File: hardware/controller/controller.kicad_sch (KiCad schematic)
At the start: 14 parts, among them J1 Conn_01x02_Pin, J2 Conn_01x02_Pin, J3 Conn_01x02_Pin, J4 Conn_01x02_Pin

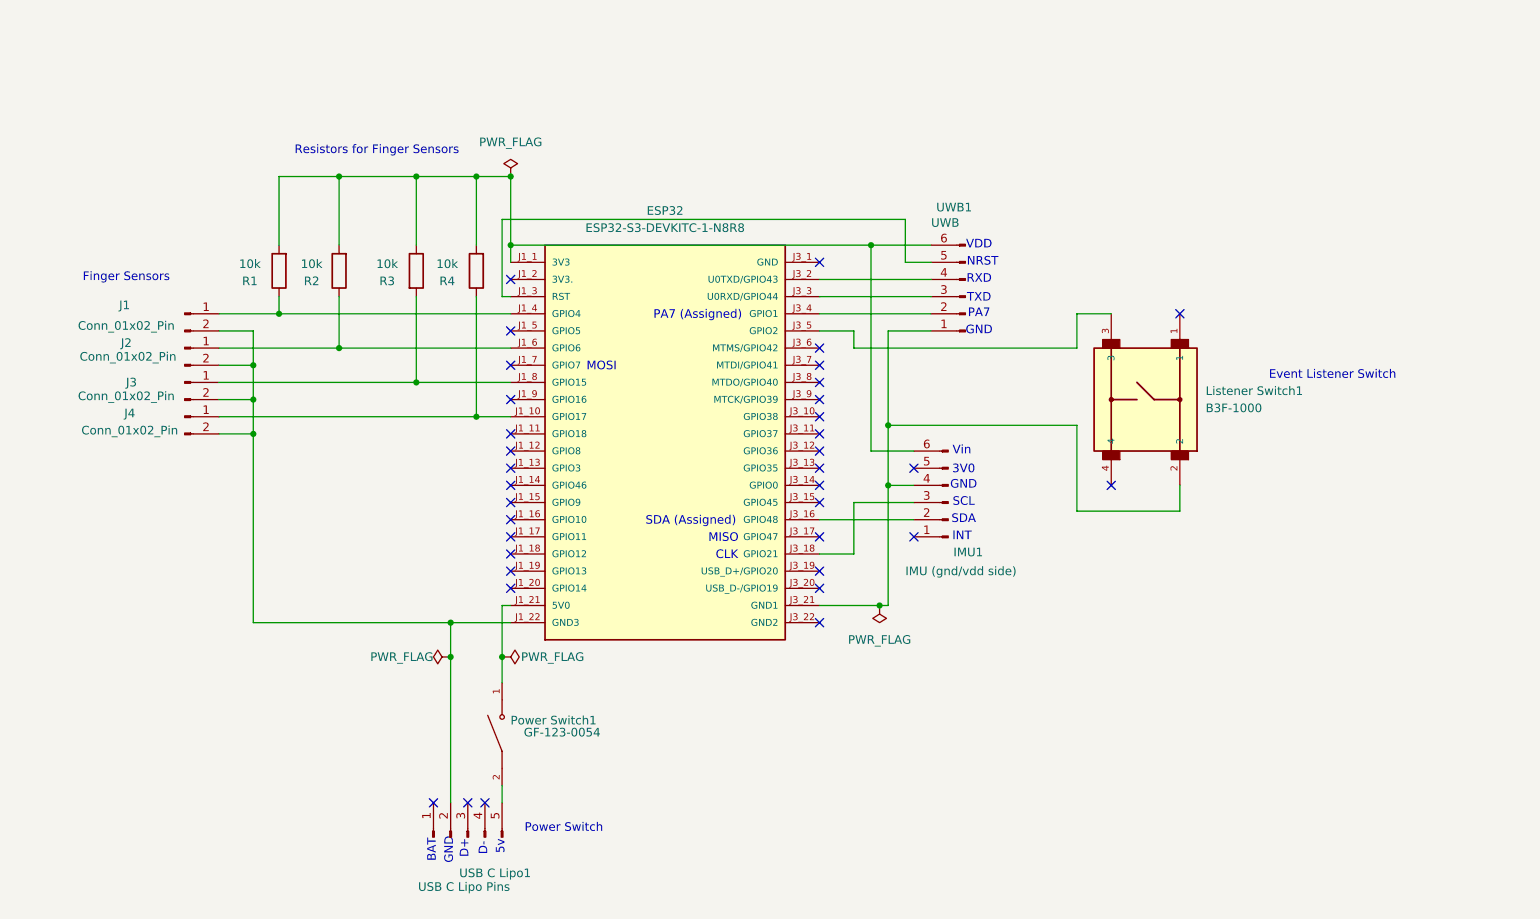
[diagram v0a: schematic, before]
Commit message: routing and screw hole placement done
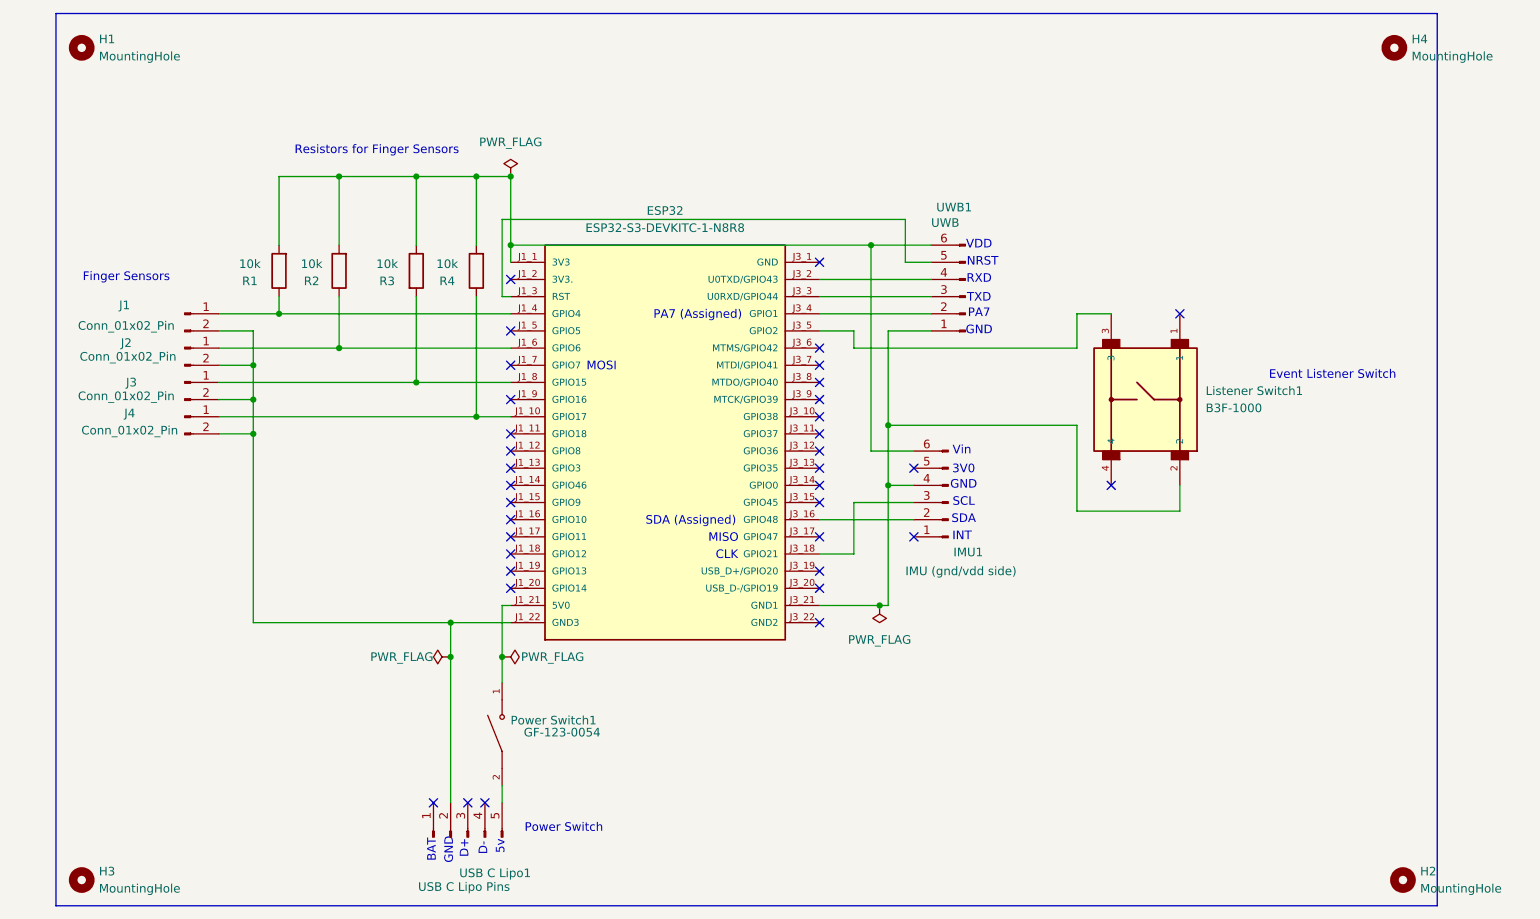
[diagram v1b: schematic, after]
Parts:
- added H1, H2, H3, H4: MountingHole, MountingHole:MountingHole_3.2mm_M3, symbol Mechanical:MountingHole

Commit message: edits made, PCB ready for 1st run
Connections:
- net at ESP32.J1_3 (RST): no longer UWB1.5 (Pin_5)
- net at ESP32.J3_2 (U0TXD/GPIO43): now also UWB1.5 (Pin_5); no longer UWB1.4 (Pin_4)
- net at ESP32.J3_3 (U0RXD/GPIO44): now also UWB1.4 (Pin_4); no longer UWB1.3 (Pin_3)
- net at ESP32.J3_4 (GPIO1): now also UWB1.3 (Pin_3); no longer UWB1.2 (Pin_2)
- net at ESP32.J3_5 (GPIO2): now also UWB1.2 (Pin_2); no longer Listener Switch1.3
- net at ESP32.J3_6 (MTMS/GPIO42): now also Listener Switch1.3
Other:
- moved on the sheet: Listener Switch1, UWB1

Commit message: added fab files
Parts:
- removed Listener Switch1: B3F-1000, B3F_1000:SW_B3F-1000, symbol B3F-1000:B3F-1000
- removed Power Switch1: GF-123-0054, GF_123_0054:SW_GF-123-0054, symbol GF-123-0054:GF-123-0054
- added Listener Switch: B3F-1000, Omron Tactile Button Small B3f-1000:SW_B3F-1000, symbol Omron Tactile Button Small:B3F-1000
- added Power Switch: GF-123-0054, On/Off Switch:SW_GF-123-0054, symbol On/Off Switch GF-123-0054:GF-123-0054
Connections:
- net at ESP32.J1_21 (5V0): now also Power Switch.1
- net at ESP32.J3_21 (GND1), IMU1.4 (Pin_4), UWB1.1 (Pin_1): now also Listener Switch.2
- net at ESP32.J3_6 (MTMS/GPIO42): now also Listener Switch.3
- net at USB C Lipo1.5 (Pin_5): now also Power Switch.2
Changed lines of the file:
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@@
+	)
+	(symbol
+		(lib_id "Omron Tactile Button Small:B3F-1000")
+		(at 364.49 195.58 90)
+		(unit 1)
+		(exclude_from_sim no)
+		(in_bom yes)
+		(on_board yes)
+		(dnp no)
+		(fields_autoplaced yes)
+		(property "Reference" "Listener Switch"
+			(at 373.38 194.3114 90)
+			(effects
+				(font
+					(size 1.27 1.27)
+				)
+				(justify right)
+			)
+		)
+		(property "Value" "B3F-1000"
+			(at 373.38 196.8514 90)
+			(effects
+				(font
+					(size 1.27 1.27)
+				)
+				(justify right)
+			)
+		)
+		(property "Footprint" "Omron Tactile Button Small B3f-1000:SW_B3F-1000"
+			(at 364.49 195.58 0)
+			(effects
+				(font
+					(size 1.27 1.27)
+				)
+				(justify bottom)
+				(hide yes)
+			)
+		)
+		(property "Datasheet" ""
+			(at 364.49 195.58 0)
+			(effects
+				(font
+					(size 1.27 1.27)
+				)
+				(hide yes)
+			)
+		)
+		(property "Description" ""
+			(at 364.49 195.58 0)
+			(effects
+				(font
+					(size 1.27 1.27)
+				)
+				(hide yes)
+			)
+		)
+		(property "MANUFACTURER" "Omron"
+			(at 364.49 195.58 0)
+			(effects
+				(font
+					(size 1.27 1.27)
+				)
+				(justify bottom)
+				(hide yes)
+			)
+		)
+		(pin "2"
+		)
+		(pin "1"
+		)
+		(pin "3"
+		)
+		(pin "4"
+		)
+		(instances
+			(project ""
+				(path "/50de191a-06b5-4968-8f0c-17f7744c4812"
+					(reference "Listener Switch")
+					(unit 1)
+				)
+			)
+		)
 	)
 	(symbol
@@
 	)
 	(symbol
+		(lib_id "On/Off Switch GF-123-0054:GF-123-0054")
+		(at 269.24 242.57 90)
+		(unit 1)
+		(exclude_from_sim no)
+		(in_bom yes)
+		(on_board yes)
+		(dnp no)
+		(fields_autoplaced yes)
+		(property "Reference" "Power Switch"
+			(at 270.51 241.2999 90)
+			(effects
+				(font
+					(size 1.27 1.27)
+				)
+				(justify right)
+			)
+		)
+		(property "Value" "GF-123-0054"
+			(at 270.51 243.8399 90)
+			(effects
+				(font
+					(size 1.27 1.27)
+				)
+				(justify right)
+			)
+		)
+		(property "Footprint" "On/Off Switch:SW_GF-123-0054"
+			(at 269.24 242.57 0)
+			(effects
+				(font
+					(size 1.27 1.27)
+				)
+				(justify bottom)
+				(hide yes)
+			)
+		)
+		(property "Datasheet" ""
+			(at 269.24 242.57 0)
+			(effects
+				(font
+					(size 1.27 1.27)
+				)
+				(hide yes)
+			)
+		)
+		(property "Description" ""
+			(at 269.24 242.57 0)
+			(effects
+				(font
+					(size 1.27 1.27)
+				)
+				(hide yes)
+			)
+		)
+		(property "PARTREV" "May 20, 2003"
+			(at 269.24 242.57 0)
+			(effects
+				(font
+					(size 1.27 1.27)
+				)
+				(justify bottom)
+				(hide yes)
+			)
+		)
+		(property "MANUFACTURER" "CW Industries"
+			(at 269.24 242.57 0)
+			(effects
+				(font
+					(size 1.27 1.27)
+				)
+				(justify bottom)
+				(hide yes)
+			)
+		)
+		(property "MAXIMUM_PACKAGE_HIEGHT" "14.96 mm"
+			(at 269.24 242.57 0)
+			(effects
+				(font
+					(size 1.27 1.27)
+				)
+				(justify bottom)
+				(hide yes)
+			)
+		)
+		(property "STANDARD" "Manufacturer Recommendations"
+			(at 269.24 242.57 0)
+			(effects
+				(font
+					(size 1.27 1.27)
+				)
+				(justify bottom)
+				(hide yes)
+			)
+		)
+		(pin "2"
+		)
+		(pin "1"
+		)
+		(instances
+			(project ""
+				(path "/50de191a-06b5-4968-8f0c-17f7744c4812"
+					(reference "Power Switch")
+					(unit 1)
+				)
+			)
+		)
+	)
+	(symbol
 		(lib_id "Connector:Conn_01x06_Pin")
 		(at 335.28 208.28 180)
@@
 	)
 	(symbol
-		(lib_id "GF-123-0054:GF-123-0054")
-		(at 269.24 242.57 90)
-		(unit 1)
-		(exclude_from_sim no)
-		(in_bom yes)
-		(on_board yes)
-		(dnp no)
-		(property "Reference" "Power Switch1"
-			(at 276.86 240.538 90)
-			(effects
-				(font
-					(size 1.27 1.27)
-				)
-			)
-		)
-		(property "Value" "GF-123-0054"
-			(at 278.13 242.316 90)
-			(effects
-				(font
-					(size 1.27 1.27)
-				)
-			)
-		)
-		(property "Footprint" "GF_123_0054:SW_GF-123-0054"
-			(at 269.24 242.57 0)
-			(effects
-				(font
-					(size 1.27 1.27)
-				)
-				(justify bottom)
-				(hide yes)
-			)
-		)
-		(property "Datasheet" ""
-			(at 269.24 242.57 0)
-			(effects
-				(font
-					(size 1.27 1.27)
-				)
-				(hide yes)
-			)
-		)
-		(property "Description" ""
-			(at 269.24 242.57 0)
-			(effects
-				(font
-					(size 1.27 1.27)
-				)
-				(hide yes)
-			)
-		)
-		(property "PARTREV" "May 20, 2003"
-			(at 269.24 242.57 0)
-			(effects
-				(font
-					(size 1.27 1.27)
-				)
-				(justify bottom)
-				(hide yes)
-			)
-		)
-		(property "MANUFACTURER" "CW Industries"
-			(at 269.24 242.57 0)
-			(effects
-				(font
-					(size 1.27 1.27)
-				)
-				(justify bottom)
-				(hide yes)
-			)
-		)
-		(property "MAXIMUM_PACKAGE_HIEGHT" "14.96 mm"
-			(at 269.24 242.57 0)
-			(effects
-				(font
-					(size 1.27 1.27)
-				)
-				(justify bottom)
-				(hide yes)
-			)
-		)
-		(property "STANDARD" "Manufacturer Recommendations"
-			(at 269.24 242.57 0)
-			(effects
-				(font
-					(size 1.27 1.27)
-				)
-				(justify bottom)
-				(hide yes)
-			)
-		)
-		(pin "1"
-		)
-		(pin "2"
-		)
-		(instances
-			(project ""
-				(path "/50de191a-06b5-4968-8f0c-17f7744c4812"
-					(reference "Power Switch1")
-					(unit 1)
-				)
-			)
-		)
-	)
-	(symbol
 		(lib_id "Mechanical:MountingHole")
 		(at 402.59 264.16 0)
@@
 					(unit 1)
 				)
-			)
-		)
-	)
-	(symbol
-		(lib_id "B3F-1000:B3F-1000")
-		(at 364.49 195.58 90)
-		(unit 1)
-		(exclude_from_sim no)
-		(in_bom yes)
-		(on_board yes)
-		(dnp no)
-		(fields_autoplaced yes)
-		(property "Reference" "Listener Switch1"
-			(at 373.38 194.3114 90)
-			(effects
-				(font
-					(size 1.27 1.27)
-				)
-				(justify right)
-			)
-		)
-		(property "Value" "B3F-1000"
-			(at 373.38 196.8514 90)
-			(effects
-				(font
-					(size 1.27 1.27)
-				)
-				(justify right)
-			)
-		)
-		(property "Footprint" "B3F_1000:SW_B3F-1000"
-			(at 364.49 195.58 0)
-			(effects
-				(font
-					(size 1.27 1.27)
-				)
-				(justify bottom)
-				(hide yes)
-			)
-		)
-		(property "Datasheet" ""
-			(at 364.49 195.58 0)
-			(effects
-				(font
-					(size 1.27 1.27)
-				)
-				(hide yes)
-			)
-		)
-		(property "Description" ""
-			(at 364.49 195.58 0)
-			(effects
-				(font
-					(size 1.27 1.27)
-				)
-				(hide yes)
-			)
-		)
-		(property "MANUFACTURER" "Omron"
-			(at 364.49 195.58 0)
-			(effects
-				(font
-					(size 1.27 1.27)
-				)
-				(justify bottom)
-				(hide yes)
-			)
-		)
-		(pin "2"
-		)
-		(pin "3"
-		)
-		(pin "1"
-		)
-		(pin "4"
-		)
-		(instances
-			(project ""
-				(path "/50de191a-06b5-4968-8f0c-17f7744c4812"
-					(reference "Listener Switch1")
-					(unit 1)
-				)

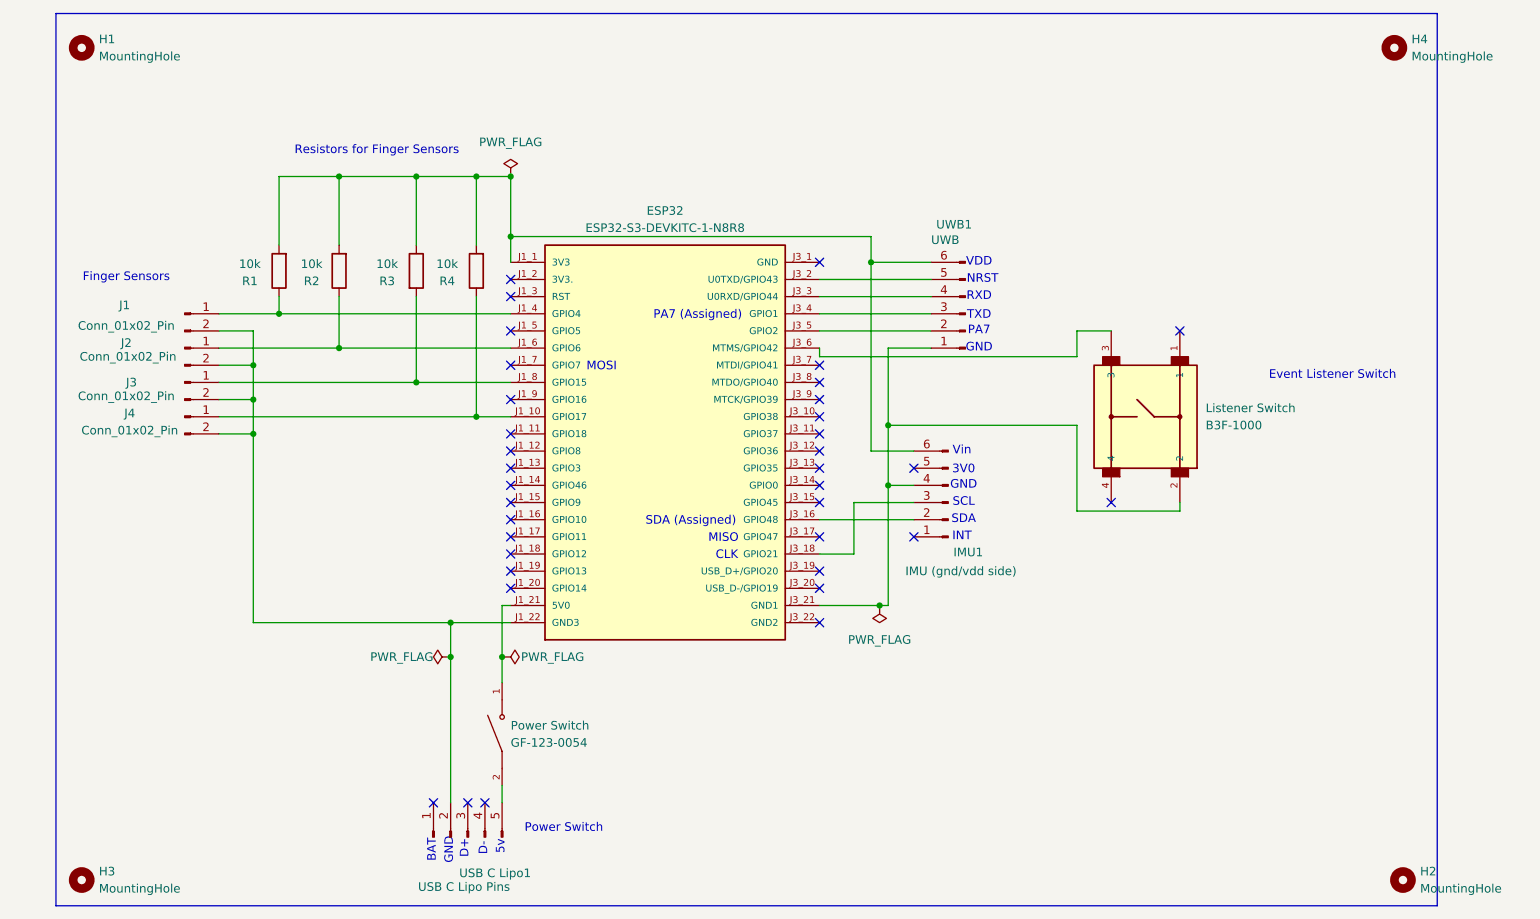
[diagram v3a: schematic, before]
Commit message: schem fixed, ready to route
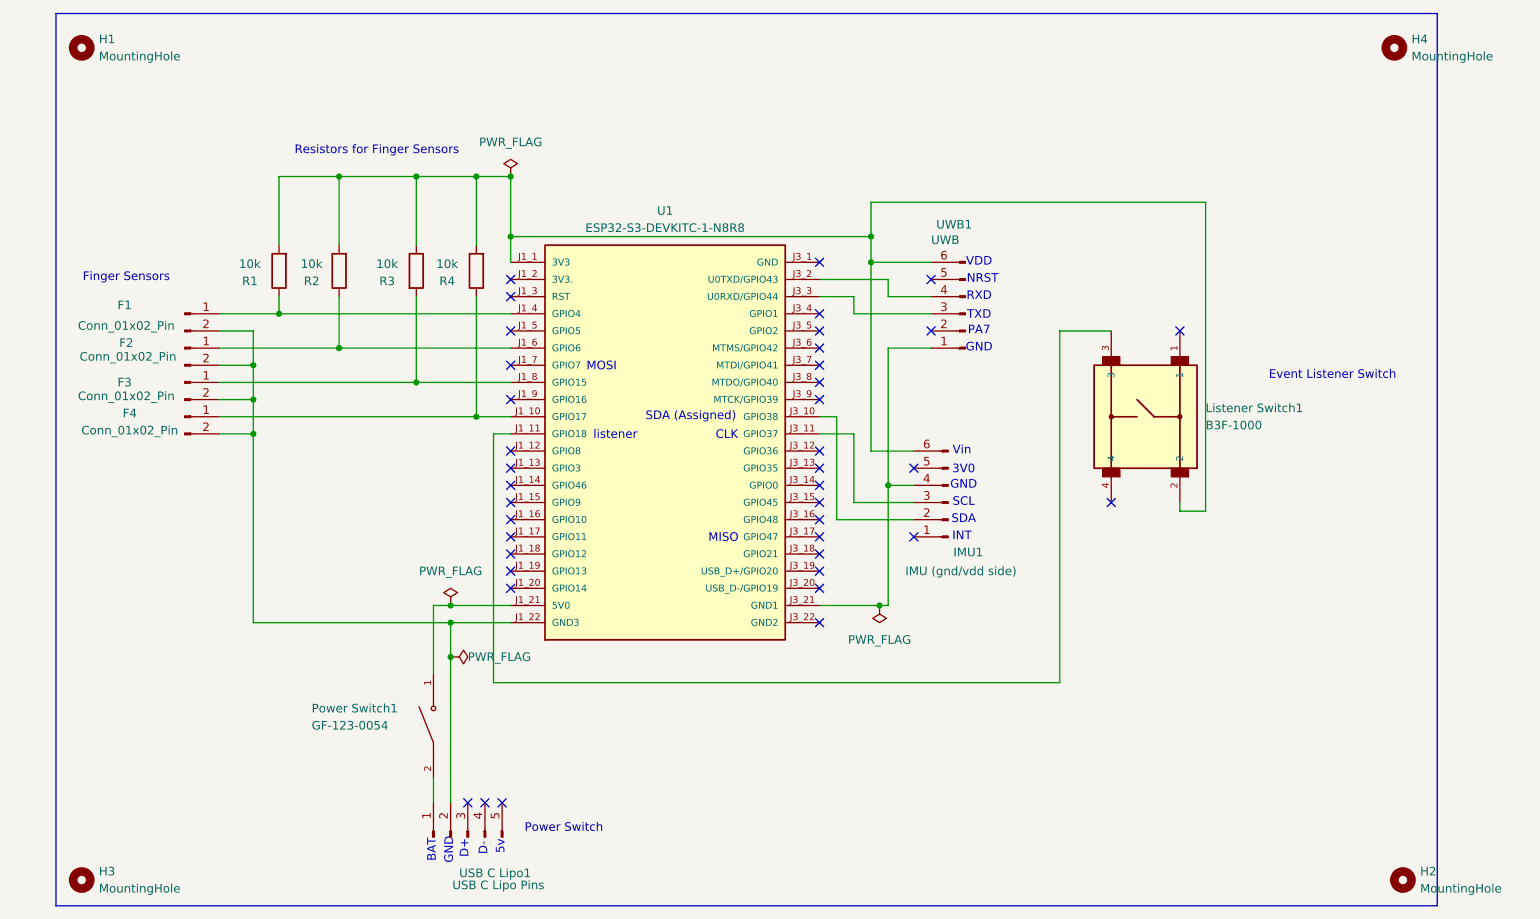
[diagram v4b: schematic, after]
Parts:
- removed ESP32: ESP32-S3-DEVKITC-1-N8R8, ESP32-S3-DEVKITC-1-N8R8:ESP32-S3-DEVKITC-1-N8R8, symbol ESP32-S3-DEVKITC-1-N8R8:ESP32-S3-DEVKITC-1-N8R8
- added U1: ESP32-S3-DEVKITC-1-N8R8, SANXIXING ESP32-S3:ESP32-S3-DEVKITC-1-N8R8, symbol SANXIXING-ESP32-S3:ESP32-S3-DEVKITC-1-N8R8
- Listener Switch1: renamed from Listener Switch
- Power Switch1: renamed from Power Switch
- renumbered J1 to F1, J2 to F2, J3 to F3, J4 to F4
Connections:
- net at F3.1 (Pin_1), R3.2: now also U1.J1_8 (GPIO15)
- net at F1.2 (Pin_2), F2.2 (Pin_2), F3.2 (Pin_2)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: now also U1.J1_22 (GND3)
- net at IMU1.6 (Pin_6), R1.2, R2.2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: now also Listener Switch1.2, U1.J1_1 (3V3)
- net at F4.1 (Pin_1), R4.1: now also U1.J1_10 (GPIO17)
- net at Power Switch1.1: now also U1.J1_21 (5V0)
- net at F1.1 (Pin_1), R1.1: now also U1.J1_4 (GPIO4)
- net at F2.1 (Pin_1), R2.1: now also U1.J1_6 (GPIO6)
- net at IMU1.2 (Pin_2): now also U1.J3_10 (GPIO38)
- net at IMU1.3 (Pin_3): now also U1.J3_11 (GPIO37)
- net at IMU1.4 (Pin_4), UWB1.1 (Pin_1): now also U1.J3_21 (GND1); no longer Listener Switch1.2
- net at UWB1.4 (Pin_4): now also U1.J3_2 (U0TXD/GPIO43)
- net at UWB1.3 (Pin_3): now also U1.J3_3 (U0RXD/GPIO44)
- net at Listener Switch1.3: now also U1.J1_11 (GPIO18)
- net at Power Switch1.2: now also USB C Lipo1.1 (Pin_1); no longer USB C Lipo1.5 (Pin_5)
- no-connect marks 36 -> 40
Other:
- note added: "listener"
- note removed: "PA7 (Assigned)"
- moved on the sheet: Power Switch1
